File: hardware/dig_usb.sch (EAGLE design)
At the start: 172 parts, among them IC1 AT90USB1287-AU, IC202 DS1337S, IC203 MAX487CSA, IC204 74HC166D, IC301 LTV-356T, IC302 LTV-356T, IC303 LTV-356T, IC304 LTV-356T, IC305 LTV-356T, IC306 LTV-356T, IC307 LTV-356T, IC308 LTV-356T, K401 S202S02, K402 S202S02, K403 S202S02, K404 S202S02, K405 S202S02, K406 S202S02, K407 S202S02, K408 S202S02, Q1 16MHz, Q201 32,768kHz, T301 BCR191, T302 BCR191, T303 BCR191, T304 BCR191, T305 BCR191, T306 BCR191, T307 BCR191, T308 BCR191, X101 RIA-73-02, X201 ISP, X202 RIA-73-02, X301 RIA-73-02, X302 RIA-73-02, X303 RIA-73-02, X304 RIA-73-02, X305 RIA-73-02, X401 RIA-73-02, X402 RIA-73-02, X403 RIA-73-02, X404 RIA-73-02, X405 RIA-73-02

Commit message: Unterer Wannenstecker auf dig_usb verschoben um Platz für Wärmebrücke zu machen
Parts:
- removed G102: KZH20SMD-2, batterie:KZH20SMD-2
- removed X202: RIA-73-02, anschluss:RIA-73-02
- removed X3: (no value), stecker:USB-MICRO-SMD-V
- added G401: TME2405S, schaltregler:TME2405S
- added X406, X407: RIA-73-02, anschluss:RIA-73-02
- G101: value TME2405S -> KZH20SMD-2; device schaltregler:TME2405S -> batterie:KZH20SMD-2; MPN TME 2405S -> (none); OC_FARNELL 1007547 -> (none); OC_NEWARK 51R5329 -> (none)
- X101: value RIA-73-02 -> (none); device anschluss:RIA-73-02 -> stecker:USB-MICRO-SMD-V
- renumbered IC1 to IC101, IC203 to IC103, IC204 to IC102, S201 to S101, X2 to X306, X201 to X102, X4 to X103
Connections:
- net GND: now also G101.-, G401.-VOUT, X101.GND; no longer G101.-VOUT, G102.-, X3.GND
- net L: now also X403.1.A, X403.2.A; no longer X401.1.A, X401.2.A
- net N$119: now also X101.D+; no longer X3.D+
- net N$121: now also X101.D-; no longer X3.D-
- net N$123: now also X101.ID; no longer X3.ID
- net N$124: now also X101.VBUS; no longer X3.VBUS
- net N$133: now also X402.2.A; no longer X202.2.A
- net N$134: now also X402.1.A; no longer X202.1.A
- net N$143: now also G101.+; no longer G102.+
- net N$19: now also G401.-VIN, X401.2.A; no longer G101.-VIN, X101.2.A
- net N$23: now also G401.+VIN; no longer G101.+VIN
- net N$24: now also X401.1.A; no longer X101.1.A
- net N$41: now also G401.+VOUT; no longer G101.+VOUT
- net N$68: now also X404.1.A; no longer X402.1.A
- net N$72: now also X404.2.A; no longer X402.2.A
- net N$74: now also X405.1.A; no longer X403.1.A
- net N$76: now also X405.2.A; no longer X403.2.A
- net N$78: now also X406.1.A; no longer X404.1.A
- net N$82: now also X406.2.A; no longer X404.2.A
- net N$84: now also X407.1.A; no longer X405.1.A
- net N$89: now also X407.2.A; no longer X405.2.A
- net USHIELD: now also X101.SHIELD; no longer X3.SHIELD

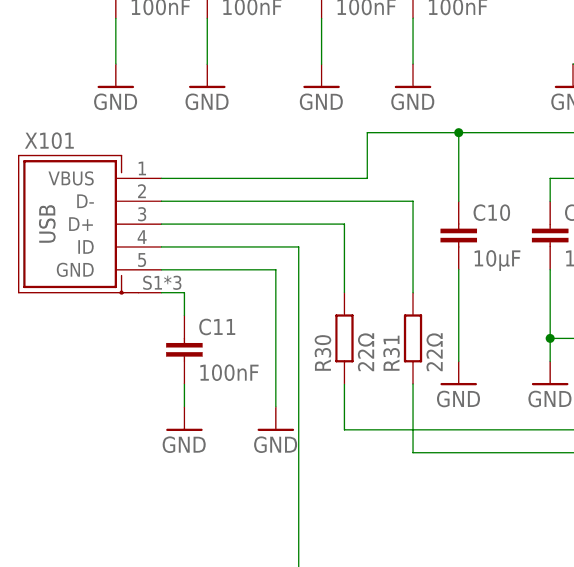
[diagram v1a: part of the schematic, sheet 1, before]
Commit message: USB Buchse ausgetauscht
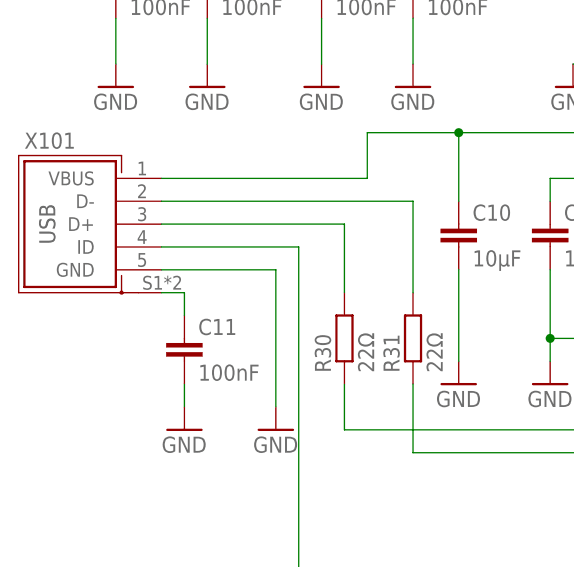
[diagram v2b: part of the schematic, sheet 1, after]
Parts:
- X101: device stecker:USB-MICRO-SMD-V -> stecker:USB-MINI-V
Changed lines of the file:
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@@
 <part name="C9" library="passiv" deviceset="C_" device="0805" value="1μF"/>
 <part name="GND67" library="versorgung" deviceset="GND" device=""/>
-<part name="X101" library="stecker" deviceset="USB-MICRO" device="-SMD-V"/>
+<part name="X101" library="stecker" deviceset="USB-MINI" device="-V"/>
 <part name="R30" library="passiv" deviceset="R_" device="0805" value="22Ω"/>
 <part name="R31" library="passiv" deviceset="R_" device="0805" value="22Ω"/>

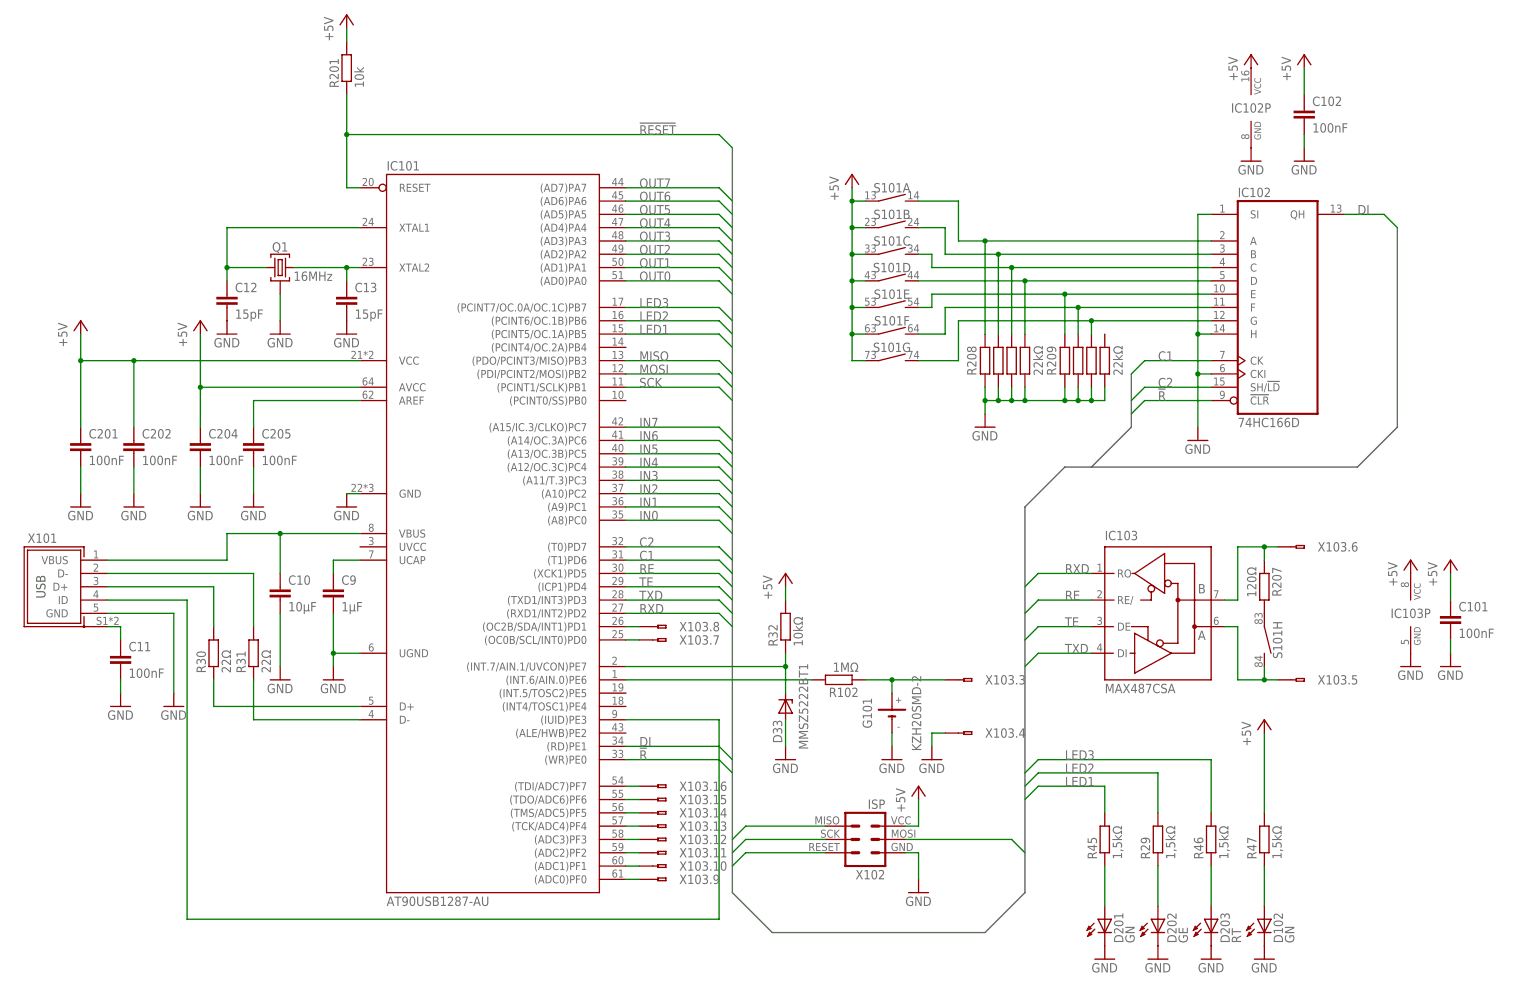
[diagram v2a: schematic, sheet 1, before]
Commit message: UVCC und HWB angeschlossen
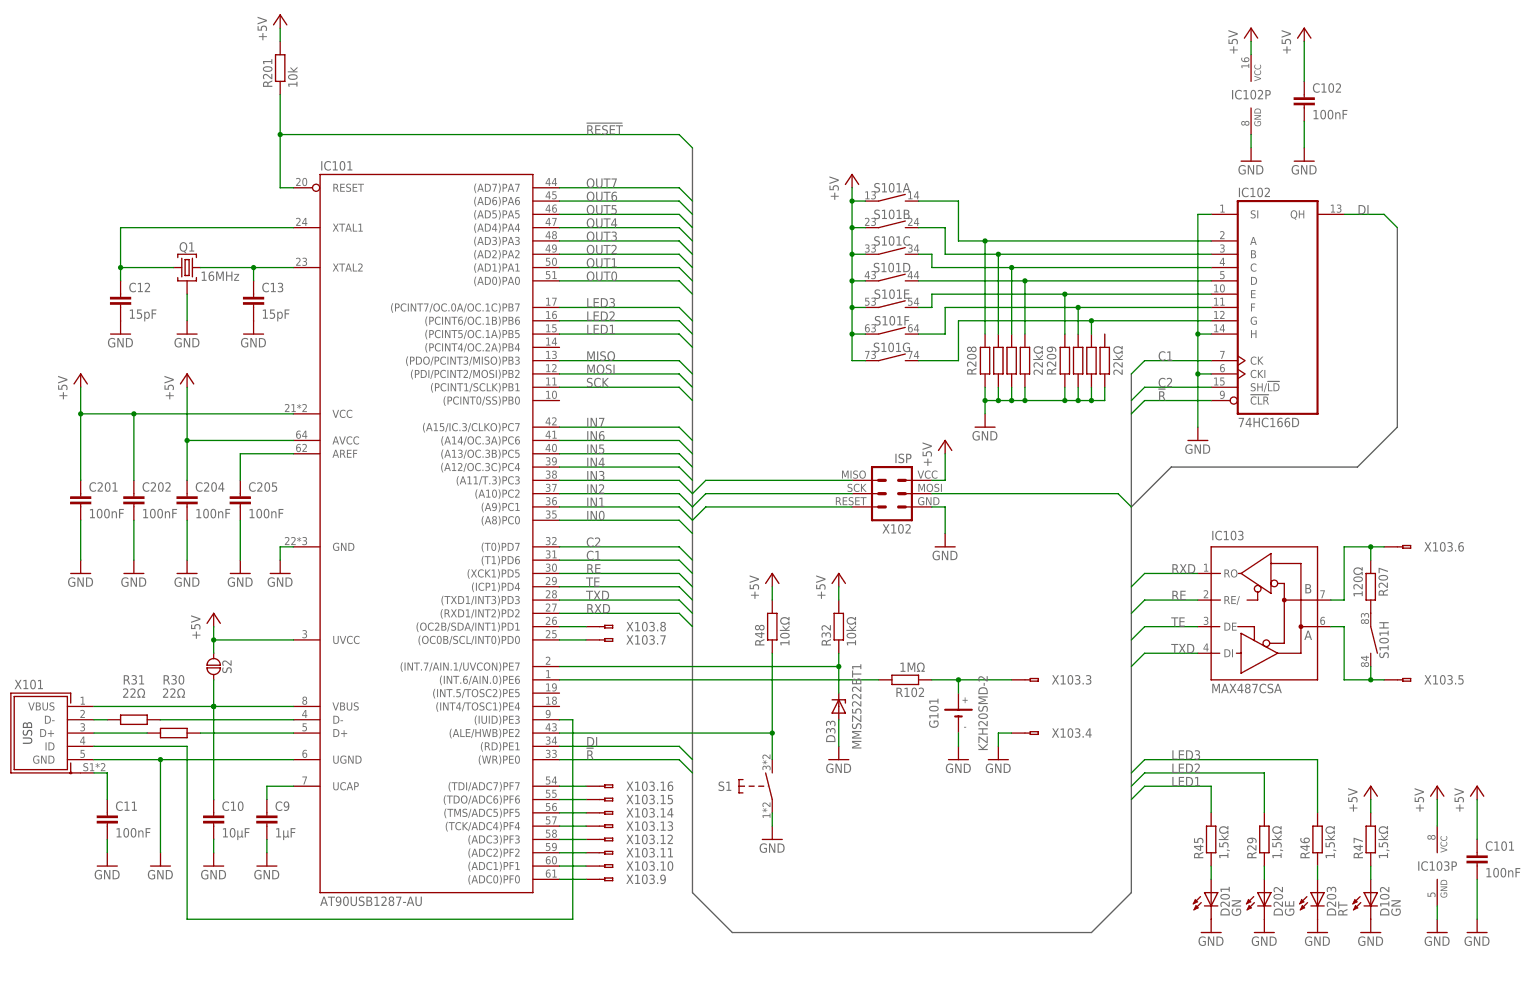
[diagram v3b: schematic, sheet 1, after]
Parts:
- added R48: 10kΩ, passiv:R_0805
- added S1: (no value), schalter:KURZHUBS1
- added S2: (no value), schalter:JUMPER
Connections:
- new net N$147: IC101.(ALE/HWB)PE2, R48.1, S1.S
- net +5V: now also IC101.UVCC, R48.2, S2.P$1
- net GND: now also S1.P
- net N$119: now also R30.1; no longer R30.2
- net N$120: now also R30.2; no longer R30.1
- net N$121: now also R31.1; no longer R31.2
- net N$122: now also R31.2; no longer R31.1
- net N$124: now also S2.P$2
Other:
- moved on the sheet: C10, C101, C102, C11, C12, C13, C201, C202, C204, C205, C9, D102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

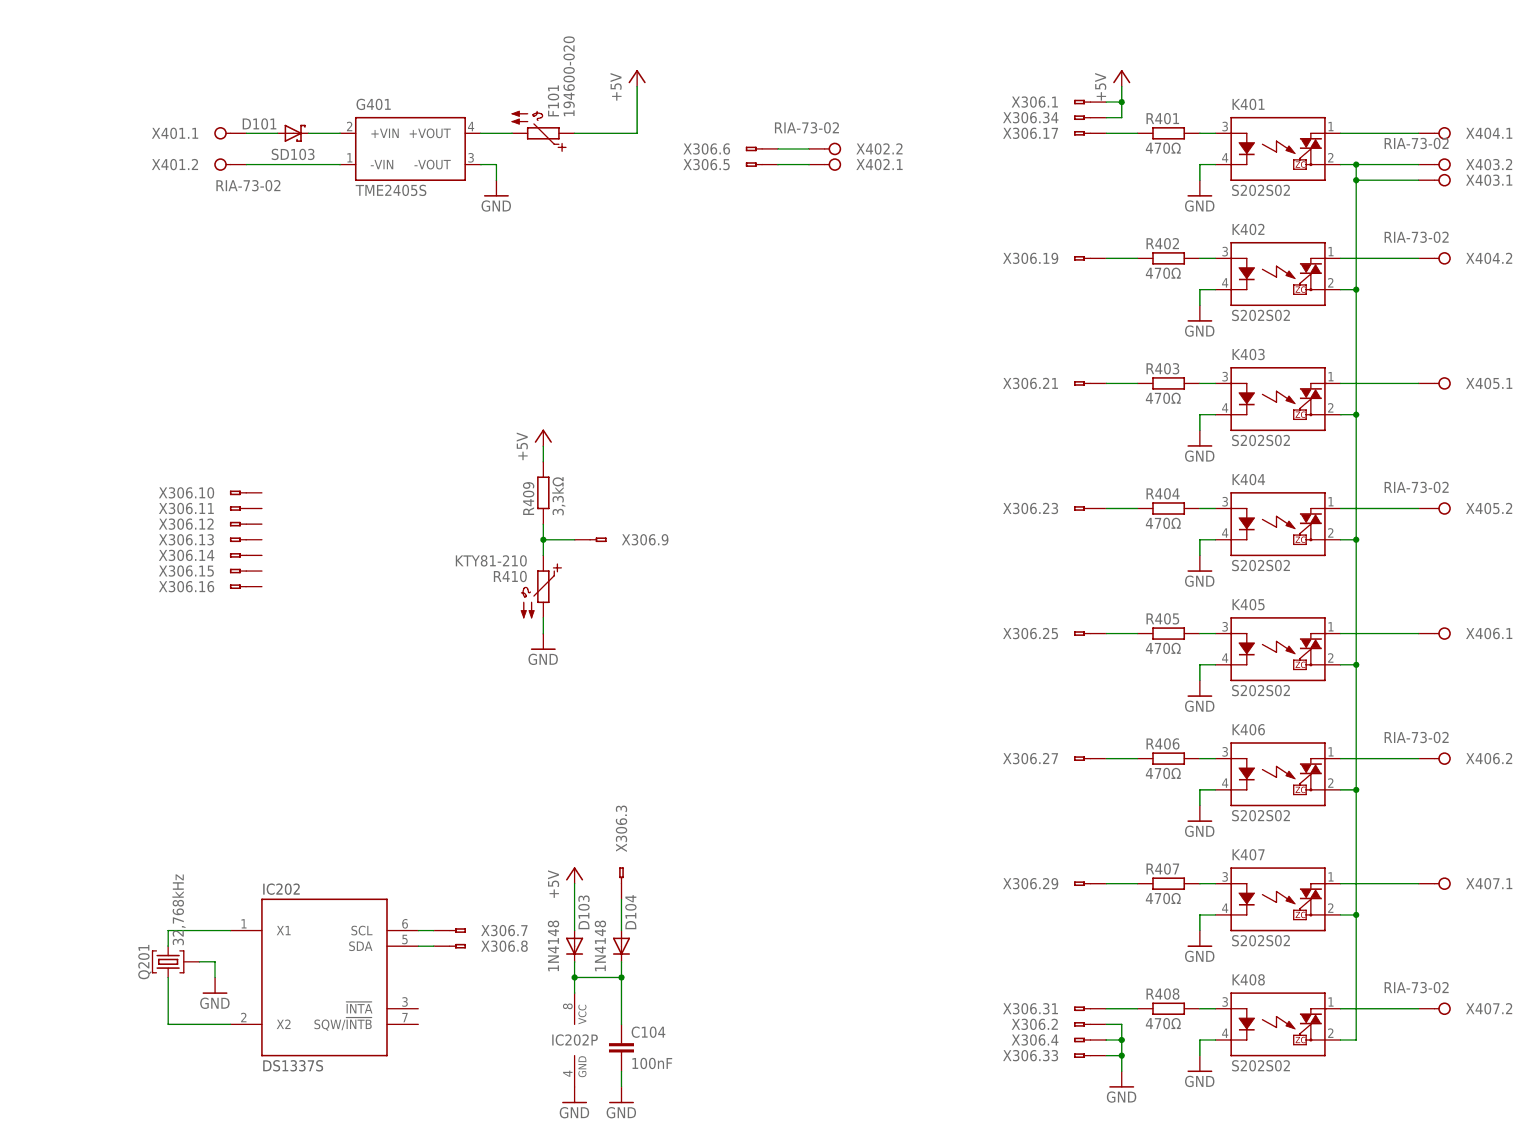
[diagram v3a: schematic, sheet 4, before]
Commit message: Steckbare Anschlüsse zu dig_usb hinzugefügt
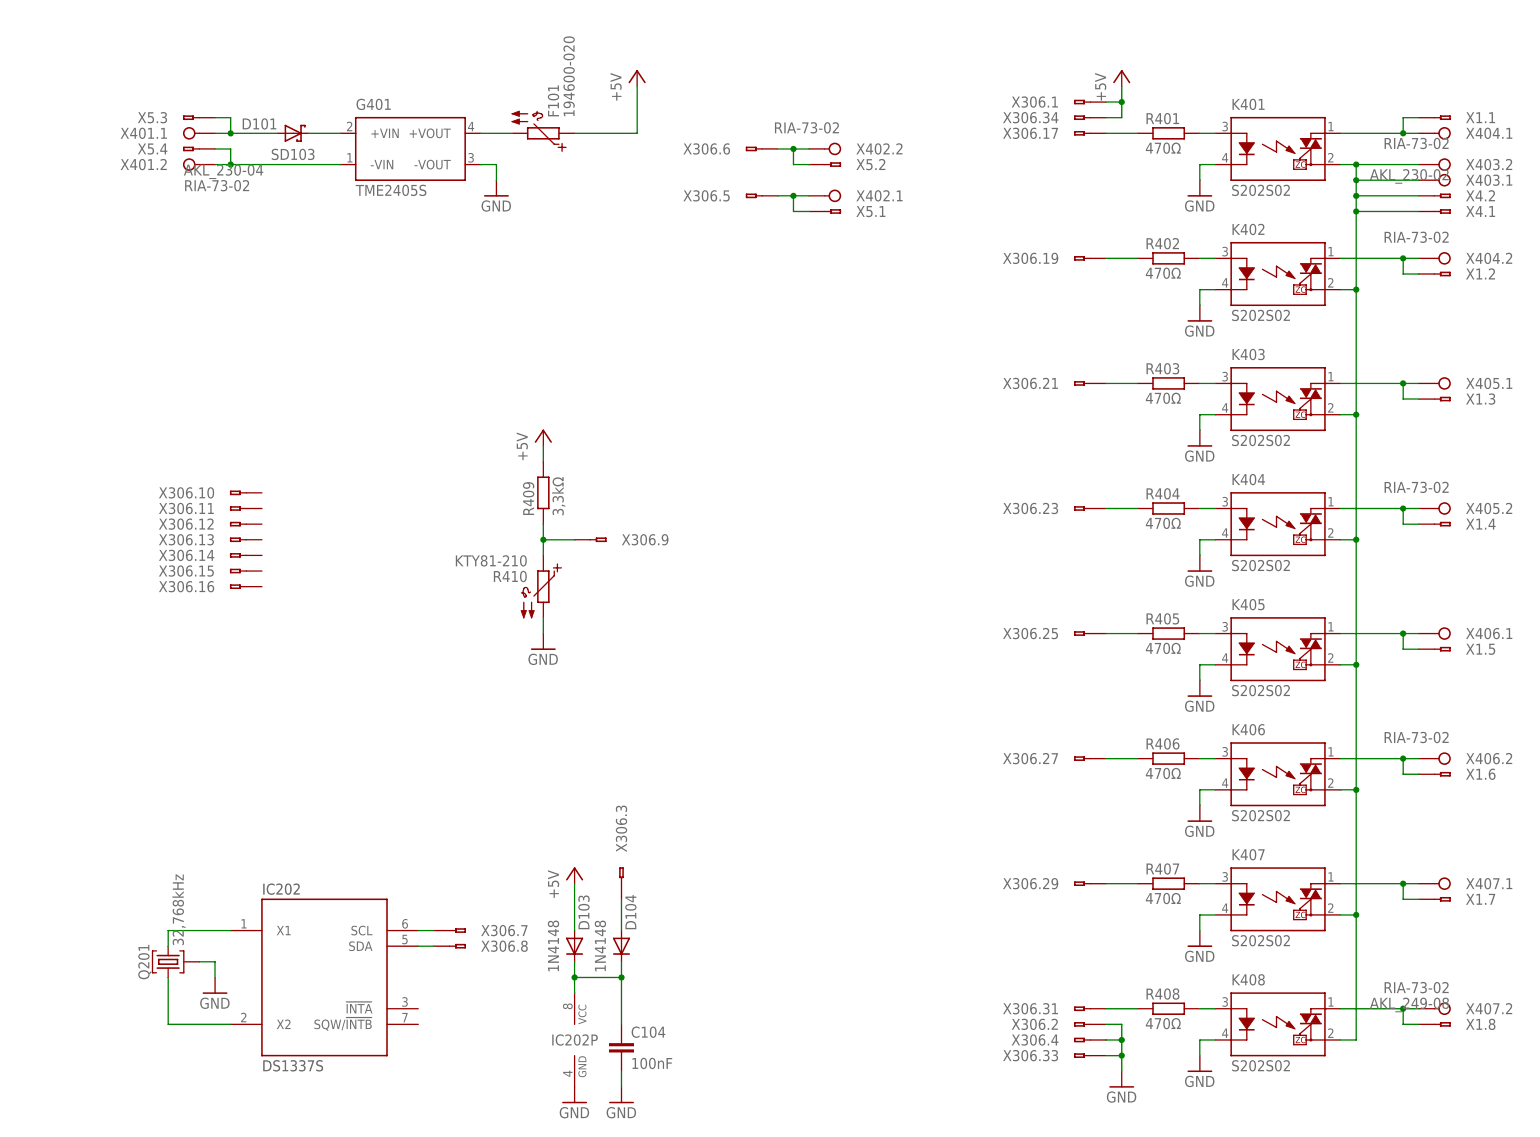
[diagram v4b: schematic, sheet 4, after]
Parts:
- added X1, X2: AKL_249-08, anschluss:AKL_249-08
- added X3, X4: AKL_230-02, anschluss:AKL_230-02
- added X5: AKL_230-04, anschluss:AKL_230-04
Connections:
- net GNDIO: now also X3.1.A, X3.2.A
- net L: now also X4.1.A, X4.2.A
- net N$133: now also X5.2.A
- net N$134: now also X5.1.A
- net N$19: now also X5.4.A
- net N$24: now also X5.3.A
- net N$45: now also X2.7.A
- net N$46: now also X2.8.A
- net N$47: now also X2.5.A
- net N$48: now also X2.6.A
- net N$56: now also X2.4.A
- net N$58: now also X2.3.A
- net N$59: now also X2.1.A
- net N$60: now also X2.2.A
- net N$68: now also X1.1.A
- net N$72: now also X1.2.A
- net N$74: now also X1.3.A
- net N$76: now also X1.4.A
- net N$78: now also X1.5.A
- net N$82: now also X1.6.A
- net N$84: now also X1.7.A
- net N$89: now also X1.8.A
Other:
- moved on the sheet: X301.1, X301.2, X302.1, X302.2, X303.1, X303.2, X304.1, X304.2, X305.1, X305.2, X306.5, X401.1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
